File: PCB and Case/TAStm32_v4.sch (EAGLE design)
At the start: 55 parts, among them CN1 330pF, CN2 330pF, CN3 330pF, CN4 330pF, IC1 74LVC3G17DP, IC2 74LVC3G17DP, IC3 74AXP4T245, IC4 74AXP4T245, J1 ZX62D-B-5PA8, J10 RJSSE538002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

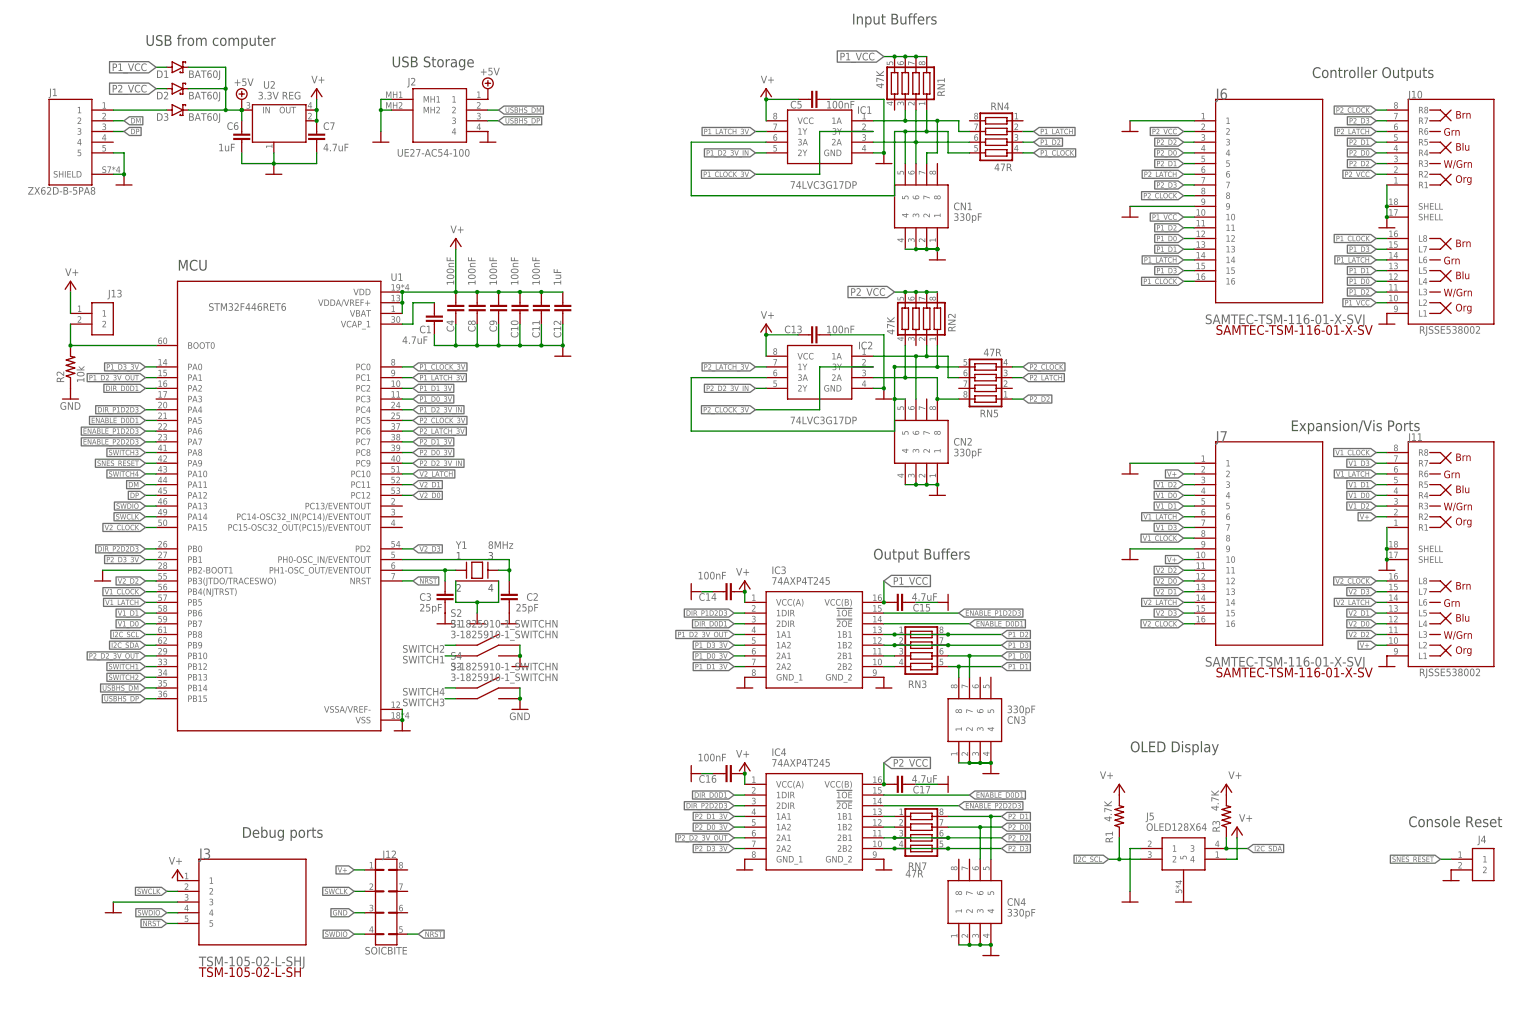
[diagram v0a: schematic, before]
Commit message: Set input filter caps to DNP
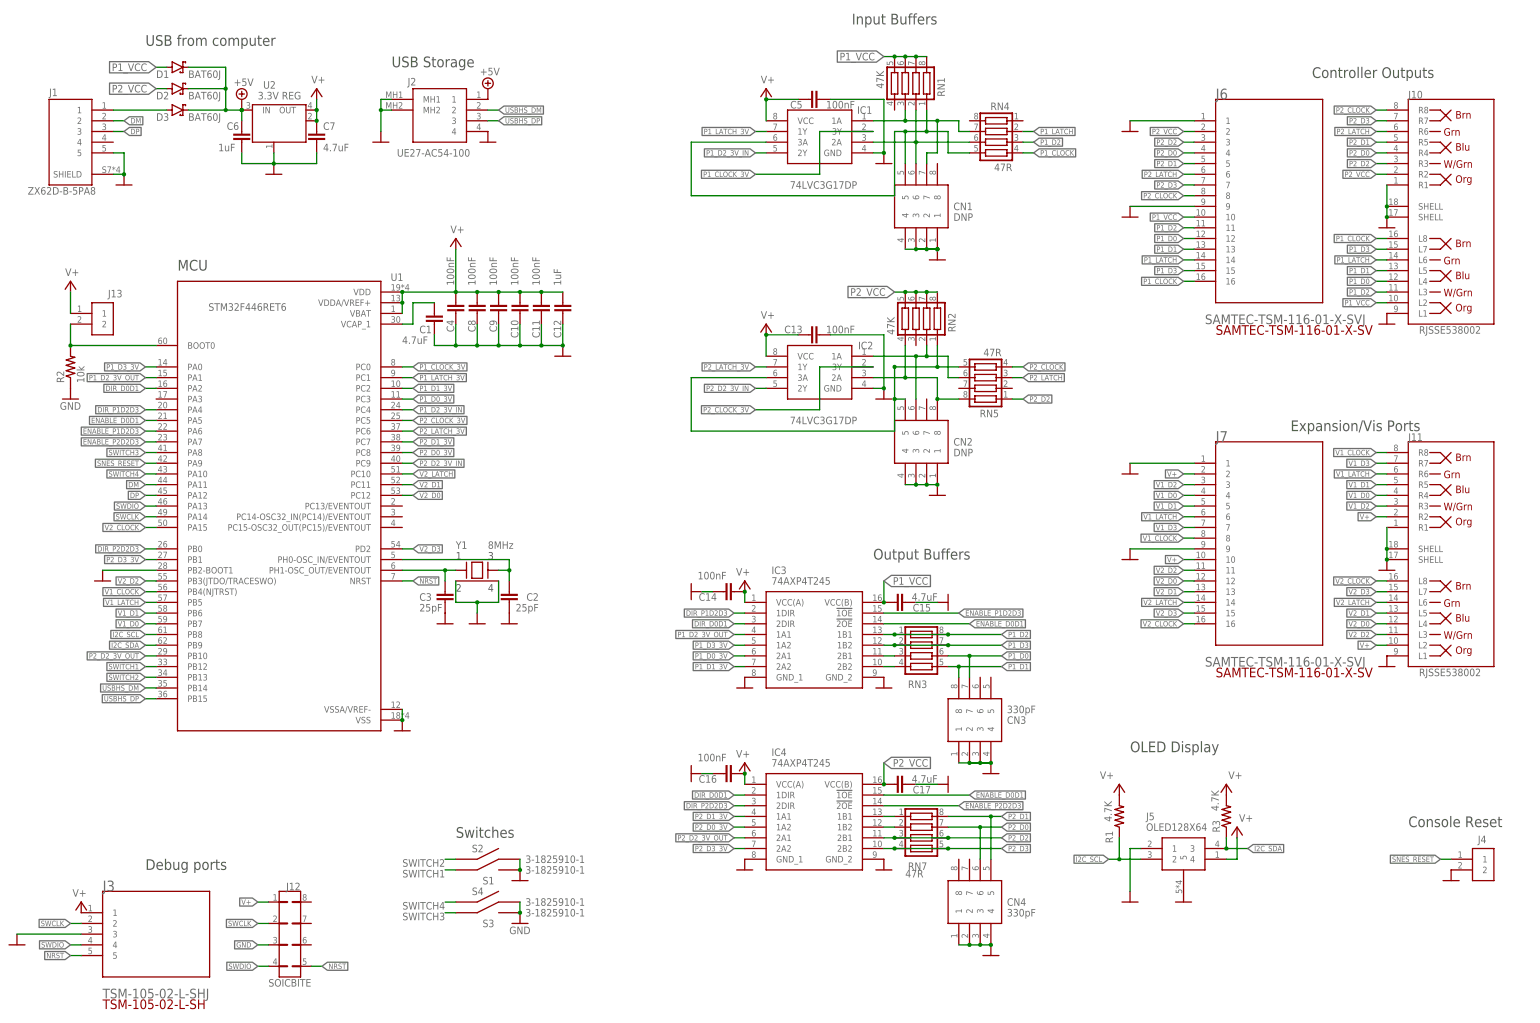
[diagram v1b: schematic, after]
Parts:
- CN1, CN2: value 330pF -> DNP
- S1, S2, S3, S4: value 3-1825910-1_SWITCHN -> 3-1825910-1
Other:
- note added: "Switches"
- moved on the sheet: J12, J3, S1, S2, S3, S4
